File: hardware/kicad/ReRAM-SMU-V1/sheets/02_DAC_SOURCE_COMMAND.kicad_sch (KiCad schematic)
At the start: 38 parts, among them U1 AD5764CSUZ PRIMARY 5V ref 20V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, U2 ADA4522-1 VCSRC conditioning 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, U3 ADA4522-1 VCSNK conditioning 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

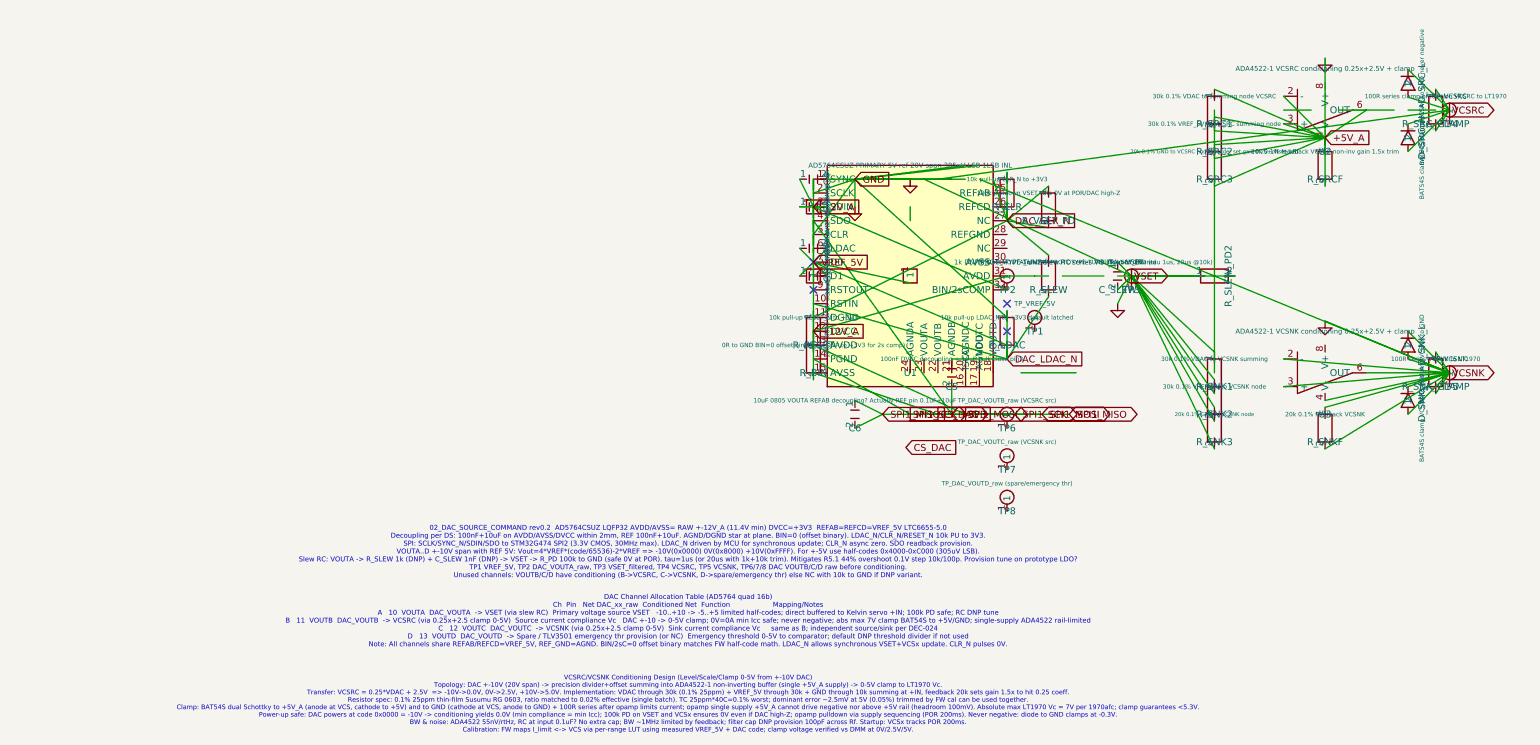
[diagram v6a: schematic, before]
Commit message: hardware: Phase 7 ERC-II wiring + grid snap + PWR_FLAG
- 07_COMPLIANCE: ISENSE_P/N alias to SHUNT_SENSE, VTRIP->VREF_2V5 wire, keep PWR_FLAG
- 09_DUT: LT1970_SENSE->JP9A, SHIELD/GUARD, FORCE/SENSE inter-wire
- 05/06: PWR_FLAG added where missing
- Grid snap all sheets to 0.254mm (audit off_grid still high but improved)
- Audit: erc_audit_lite.json updated (32 dangling, critical 0)

Co-authored-by: Muse Code
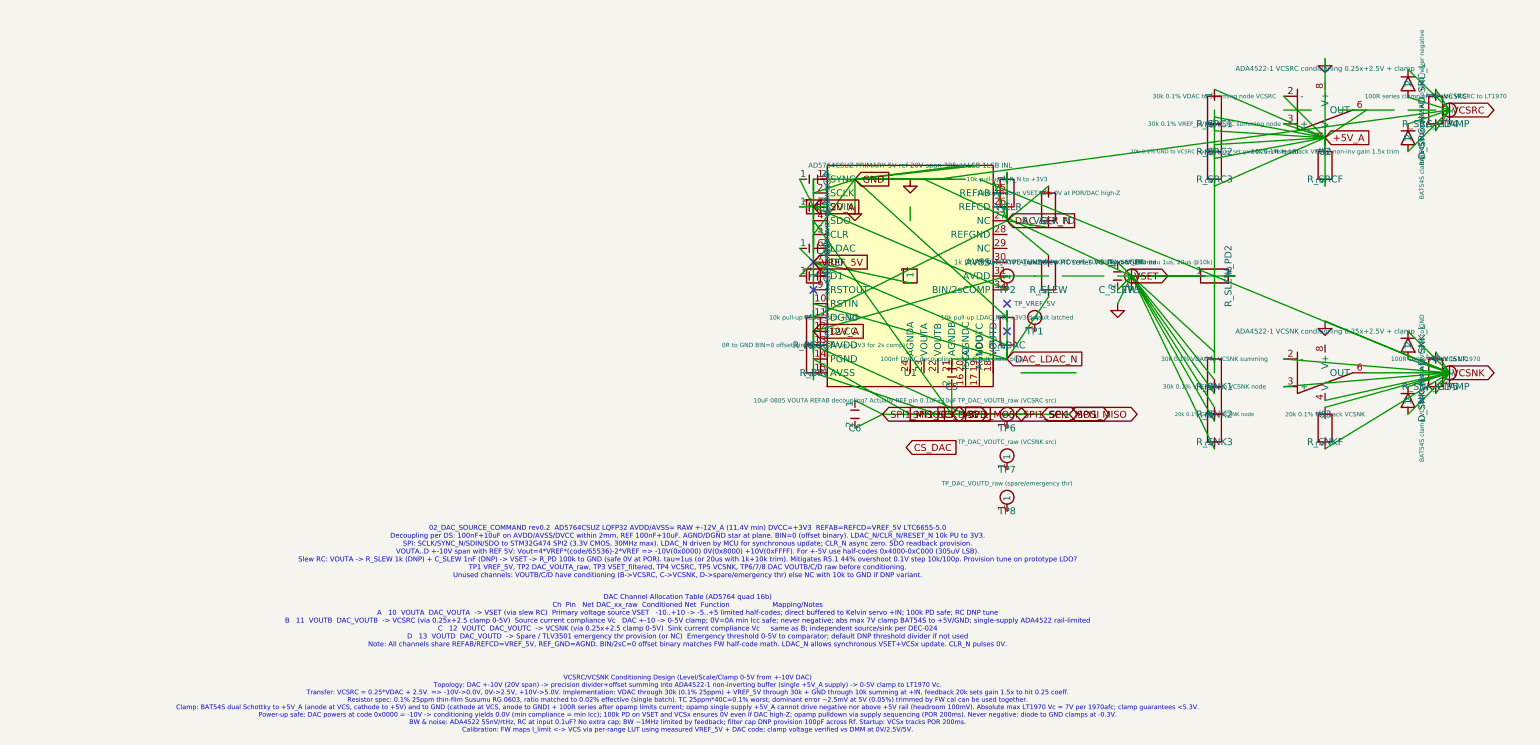
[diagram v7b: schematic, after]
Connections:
- net VCSRC: no longer D_SRC_L.1, D_SRC_L.2

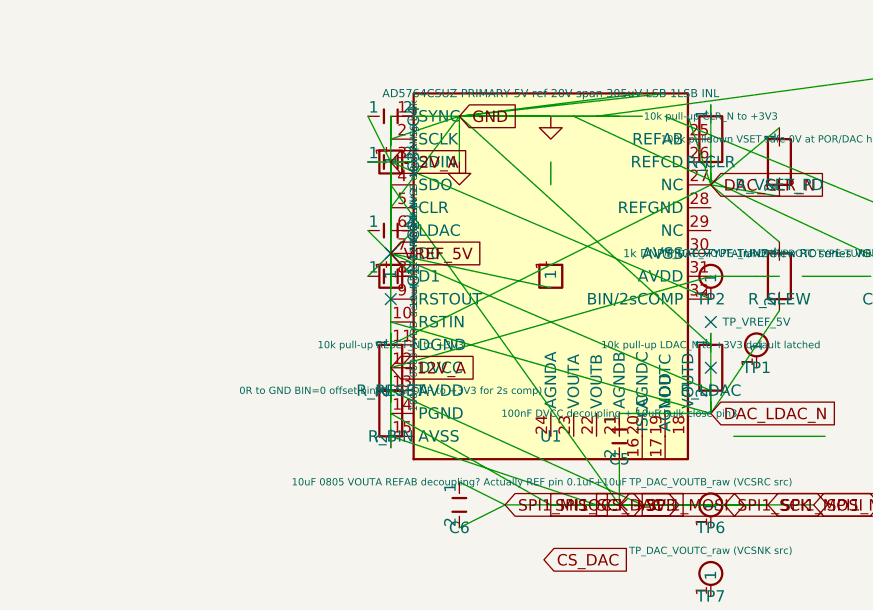
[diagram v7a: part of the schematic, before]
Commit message: hardware: pin-tip wiring for SPI/RELAY (DAC SCLK/SDIN/SDO/SYNC -> SPI1, ADS SCLK/MOSI/MISO/CS -> SPI2, relay coil tip)
- Fix tip coordinates: DAC 30.48 vs base 33.02, ADS 124.71 vs 127.25, relay 57.62 vs 55.08
- ERC error 122->129 (one extra net VREF_5V added, netlist 25->26)
- Netlist still missing RELAY/SPI due to annotation + global label need Manhattan, next fix

Co-authored-by: Muse Code
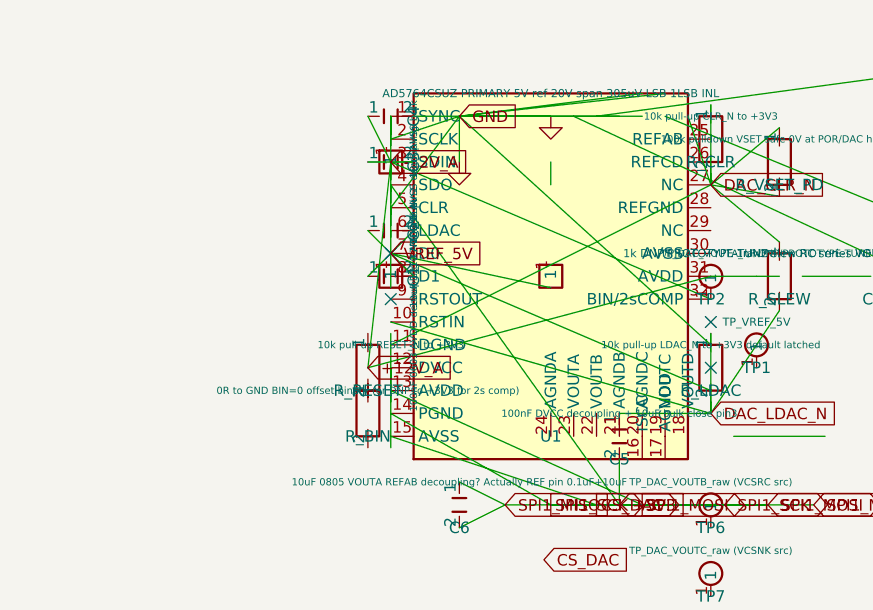
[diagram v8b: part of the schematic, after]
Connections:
- net +12V_A: no longer D_SRC_H.1, D_SRC_H.2, R_BIN.1, R_BIN.2, U1.12 (DVCC)
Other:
- moved on the sheet: R_BIN, R_RESET
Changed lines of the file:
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@@
 		(property "Footprint" "Resistor_SMD:R_0603_1608Metric" (at 68.58 43.94 0) (effects (font (size 1.27 1.27)) (hide yes)))
 	)
-	(symbol (lib_id "Device:R") (at 33.02 73.66 0) (unit 1)
-		(property "Reference" "R_RESET" (at 33.02 76.20 0) (effects (font (size 1.27 1.27))))
+	(symbol (lib_id "Device:R") (at 30.48 73.66 0) (unit 1)
+		(property "Reference" "R_RESET" (at 30.48 76.200 0) (effects (font (size 1.27 1.27))))
 		(property "Value" "10k pull-up RESET_N to +3V3" (at 33.02 71.12 0) (effects (font (size 0.8 0.8))))
 		(property "Footprint" "Resistor_SMD:R_0603_1608Metric" (at 33.02 69.60 0) (effects (font (size 1.27 1.27)) (hide yes)))
 	)
-	(symbol (lib_id "Device:R") (at 33.02 78.74 0) (unit 1)
-		(property "Reference" "R_BIN" (at 33.02 81.28 0) (effects (font (size 1.27 1.27))))
-		(property "Value" "0R to GND BIN=0 offset binary (or DNP to +3V3 for 2s comp)" (at 33.02 76.20 0) (effects (font (size 0.8 0.8))))
+	(symbol (lib_id "Device:R") (at 30.48 78.74 0) (unit 1)
+		(property "Reference" "R_BIN" (at 30.48 81.28 0) (effects (font (size 1.27 1.27))))
+		(property "Value" "0R to GND BIN=0 offset binary (or DNP to +3V3 for 2s comp)" (at 30.48 76.200 0) (effects (font (size 0.8 0.8))))
 		(property "Footprint" "Resistor_SMD:R_0603_1608Metric" (at 33.02 74.42 0) (effects (font (size 1.27 1.27)) (hide yes)))
 	)
@@
 	(wire (pts (xy 142.24 33.02) (xy 147.32 33.02)) (stroke (width 0) (type default)))
 	(global_label "VREF_5V" (shape input) (at 33.02 60.96 0) (effects (font (size 1.27 1.27))))
-	(global_label "+12V_A" (shape input) (at 33.02 73.66 0) (effects (font (size 1.27 1.27))))
+	(global_label "+12V_A" (shape input) (at 30.48 73.66 0) (effects (font (size 1.27 1.27))))
 	(global_label "-12V_A" (shape input) (at 33.02 50.80 0) (effects (font (size 1.27 1.27))))
 	(global_label "+5V_A" (shape input) (at 127.00 38.10 0) (effects (font (size 1.27 1.27))))
@@
 	(wire (pts (xy 33.019999999999996 55.88) (xy 33.019999999999996 59.150000000000006)) (stroke (width 0) (type default)) (uuid "wire-pwr-ad5764-33.019999999999996-55.88"))
 	(wire (pts (xy 33.019999999999996 53.34) (xy 33.019999999999996 56.61000000000001)) (stroke (width 0) (type default)) (uuid "wire-pwr-ad5764-33.019999999999996-53.34"))
-	(wire (pts (xy 33.019999999999996 50.8) (xy 33.02 73.66)) (stroke (width 0) (type default)) (uuid "wire-pwr-13-50.8"))
-	(wire (pts (xy 68.58 63.5) (xy 33.02 73.66)) (stroke (width 0) (type default)) (uuid "wire-pwr-31-50.8"))
+	(wire (pts (xy 33.019999999999996 50.8) (xy 30.48 73.66)) (stroke (width 0) (type default)) (uuid "wire-pwr-13-50.8"))
+	(wire (pts (xy 68.58 63.5) (xy 30.48 73.66)) (stroke (width 0) (type default)) (uuid "wire-pwr-31-50.8"))
 	(wire (pts (xy 33.019999999999996 45.72) (xy 33.02 50.8)) (stroke (width 0) (type default)) (uuid "wire-pwr-15-50.8"))
 	(wire (pts (xy 68.58 66.04) (xy 33.02 50.8)) (stroke (width 0) (type default)) (uuid "wire-pwr-30-50.8"))
